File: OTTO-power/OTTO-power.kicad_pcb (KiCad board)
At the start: 2 copper layers, 72.5 x 23.5 mm, 48 parts, among them J1 Barrel_Jack, J2 Conn_01x10, J3 USB_B_Micro, J4 battery, SW1 SW_Push, SW2 SW_reset, U1 MAX8903A, U2 MAX17048, U3 TPS61090, U4 XC6210

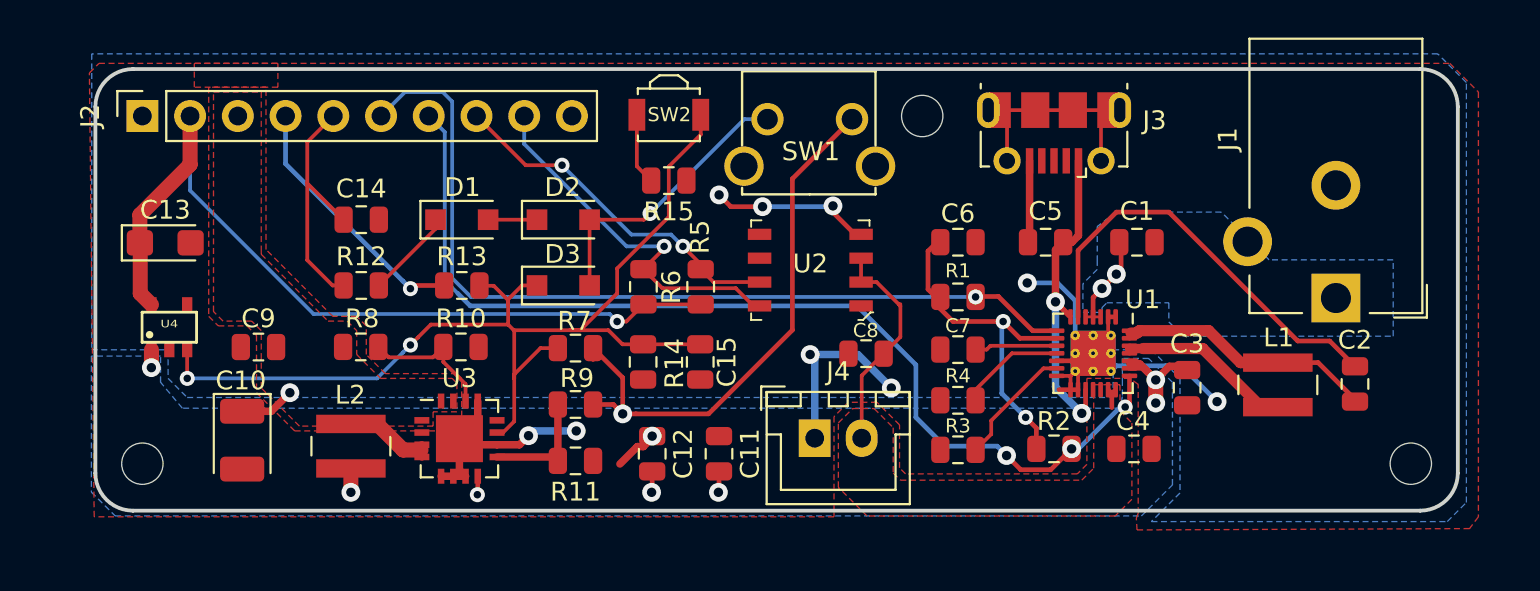
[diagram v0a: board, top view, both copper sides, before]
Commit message: New power board routing
Attempted to consolidate some of the traces and component placement for the OTTO power board. Only current outstanding item is double checking via sizing for max current load and overall QA check of board.
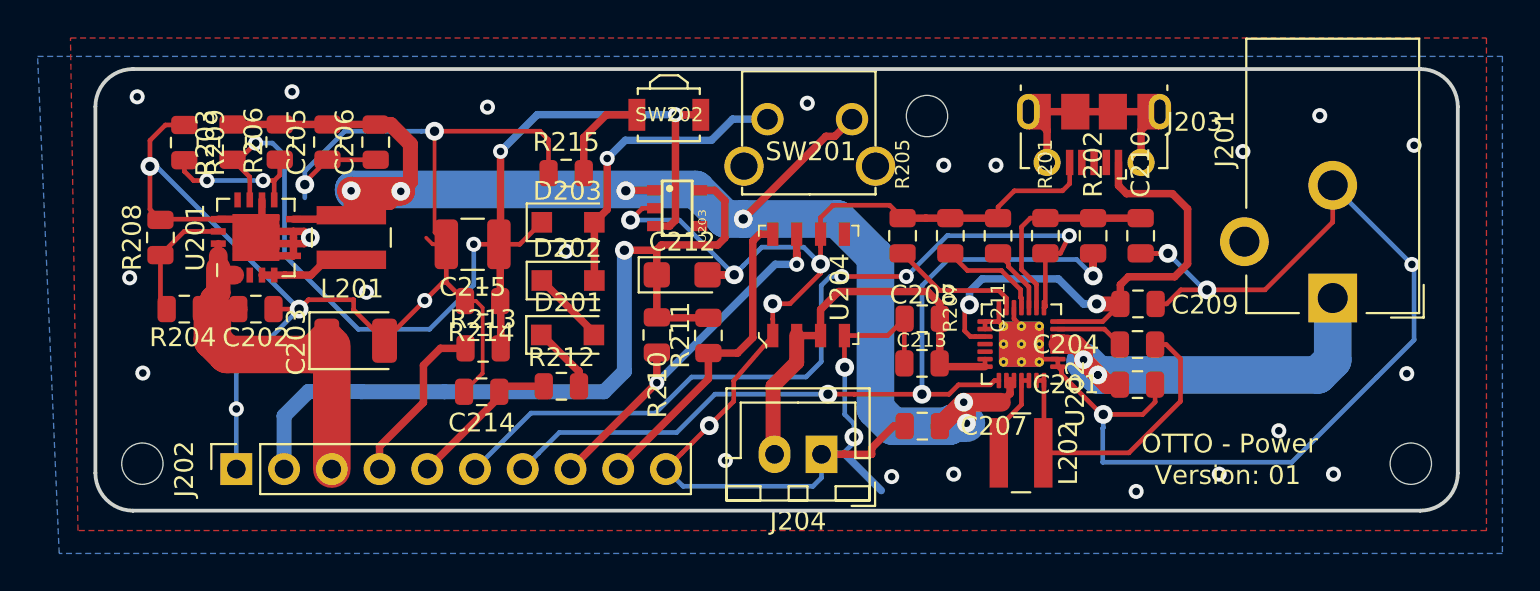
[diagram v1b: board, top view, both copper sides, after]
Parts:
- removed C15: 100uf, Capacitor_SMD:C_0805_2012Metric
- added C215: 100uf, Capacitor_SMD:C_1210_3225Metric, F.Cu at (169.6, 33.1)
- moved U203 27.8 mm to (180.4, 31.2), turned to 270 degrees
- moved C212 27.6 mm to (180.7, 34.8)
- moved R209 26.8 mm to (154.2, 27.7), turned to 270 degrees
- moved C205 26.6 mm to (161.8, 27.7), turned to 90 degrees
- moved C206 22.2 mm to (164.4, 27.7), turned to 90 degrees
- moved R203 21.3 mm to (156.8, 27.7), turned to 90 degrees
- moved R206 21.0 mm to (159.3, 27.7), turned to 90 degrees
- moved J202 19.4 mm to (157.0, 45.1)
- moved R208 17.0 mm to (152.9, 32.8), turned to 270 degrees
- moved U201 15.2 mm to (158.0, 32.8), turned to 90 degrees
- moved C207 14.2 mm to (193.5, 42.8), turned to 0 degrees
- moved L202 14.1 mm to (198.7, 44.2), turned to 0 degrees
- moved C208 13.2 mm to (193.5, 37.1), turned to 0 degrees
- moved R212 11.9 mm to (174.3, 40.7)
- moved R205 11.8 mm to (192.4, 32.7), turned to 270 degrees
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- renumbered C1 to C201, C9 to C202, C10 to C203, C2 to C204, C11 to C205, C12 to C206, C3 to C207, C4 to C208, C5 to C209, C6 to C210, C7 to C211, C13 to C212, C8 to C213, C14 to C214, D1 to D201, D2 to D202, D3 to D203, J1 to J201, J2 to J202, J3 to J203, J4 to J204, L2 to L201, L1 to L202, R1 to R201, R2 to R202, R7 to R203, R8 to R204, R3 to R205, R9 to R206, R4 to R207, R10 to R208, R11 to R209, R5 to R210, R6 to R211, R12 to R212, R13 to R213, R14 to R214, R15 to R215, SW1 to SW201, SW2 to SW202, U3 to U201, U1 to U202, U4 to U203, U2 to U204
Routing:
- net GNDA: track 58.7 -> 242.9 mm, vias 10 -> 39
- net SYS: track 43.1 -> 85.6 mm, vias 8 -> 6
- net Net-(C204-Pad1): track 22.5 -> 3.64 mm
- net 5V: track 2.95 -> 21.6 mm, vias 1 -> 0
- net DC: track 5.39 -> 22.4 mm, vias 2 -> 3
- net USB: track 17.3 -> 29.4 mm
- net BATT+: track 13.5 -> 22.9 mm
- net CHG_OUT: track 54.3 -> 45.5 mm
- net VL: track 18.8 -> 11.2 mm, vias 2 -> 0
- net SENSE_PIN: track 13.5 -> 8.19 mm
- net Net-(L202-Pad1): track 9.84 -> 4.75 mm
- net OUT_PIN: track 13.8 -> 9.10 mm, vias 1 -> 0
- net DOK_OUT: track 47.3 -> 44.0 mm, vias 1 -> 3
- net SDA: track 19.9 -> 17.2 mm, vias 1 -> 0
- net Net-(C204-Pad2): track 14.2 -> 16.6 mm
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- removed copper zone on F.Cu, net 5V
- removed copper zone on F.Cu, net BATT+
- removed copper zone on B.Cu, net DC
- removed copper zone on B.Cu, net SYS
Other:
- board text added: "OTTO - Power"
- board text added: "Version: 01"
